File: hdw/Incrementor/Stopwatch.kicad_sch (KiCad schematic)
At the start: 0 parts

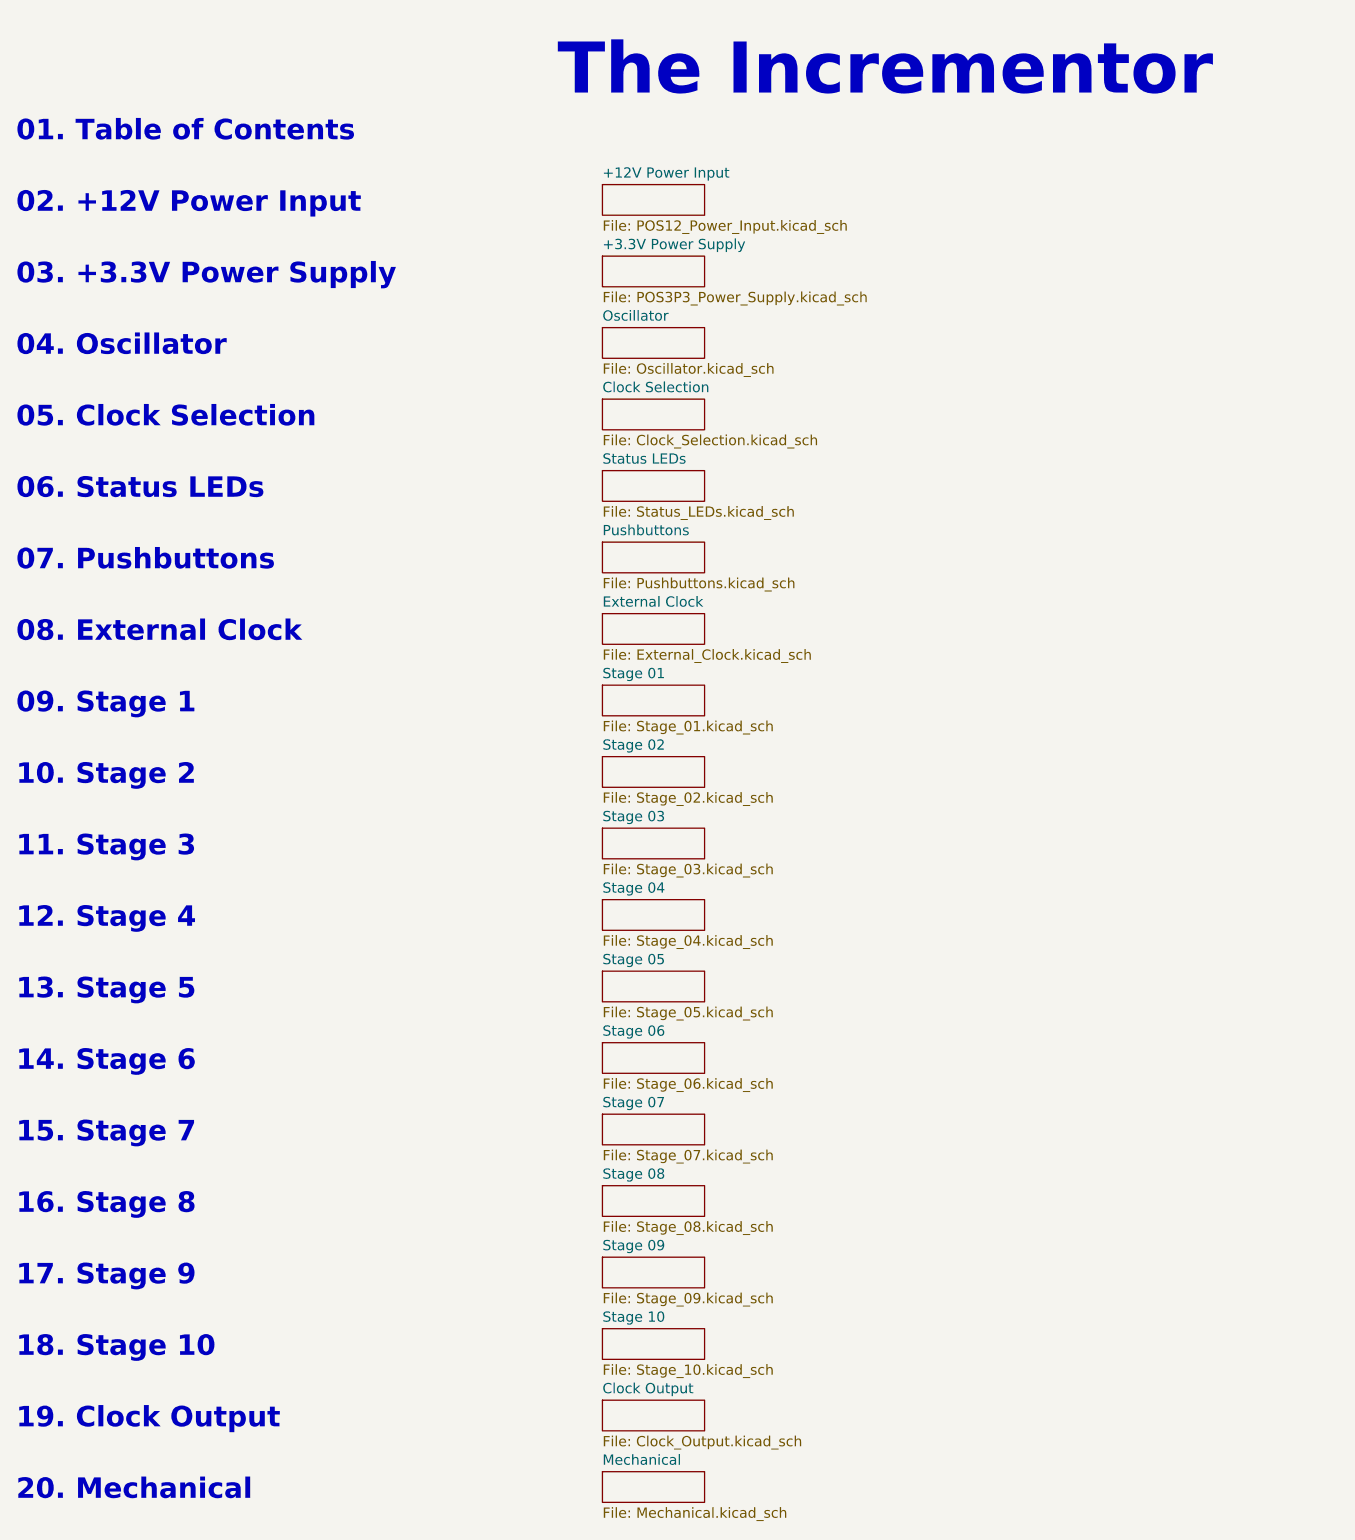
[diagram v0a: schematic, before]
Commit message: renamed project, removed stuff I dont need
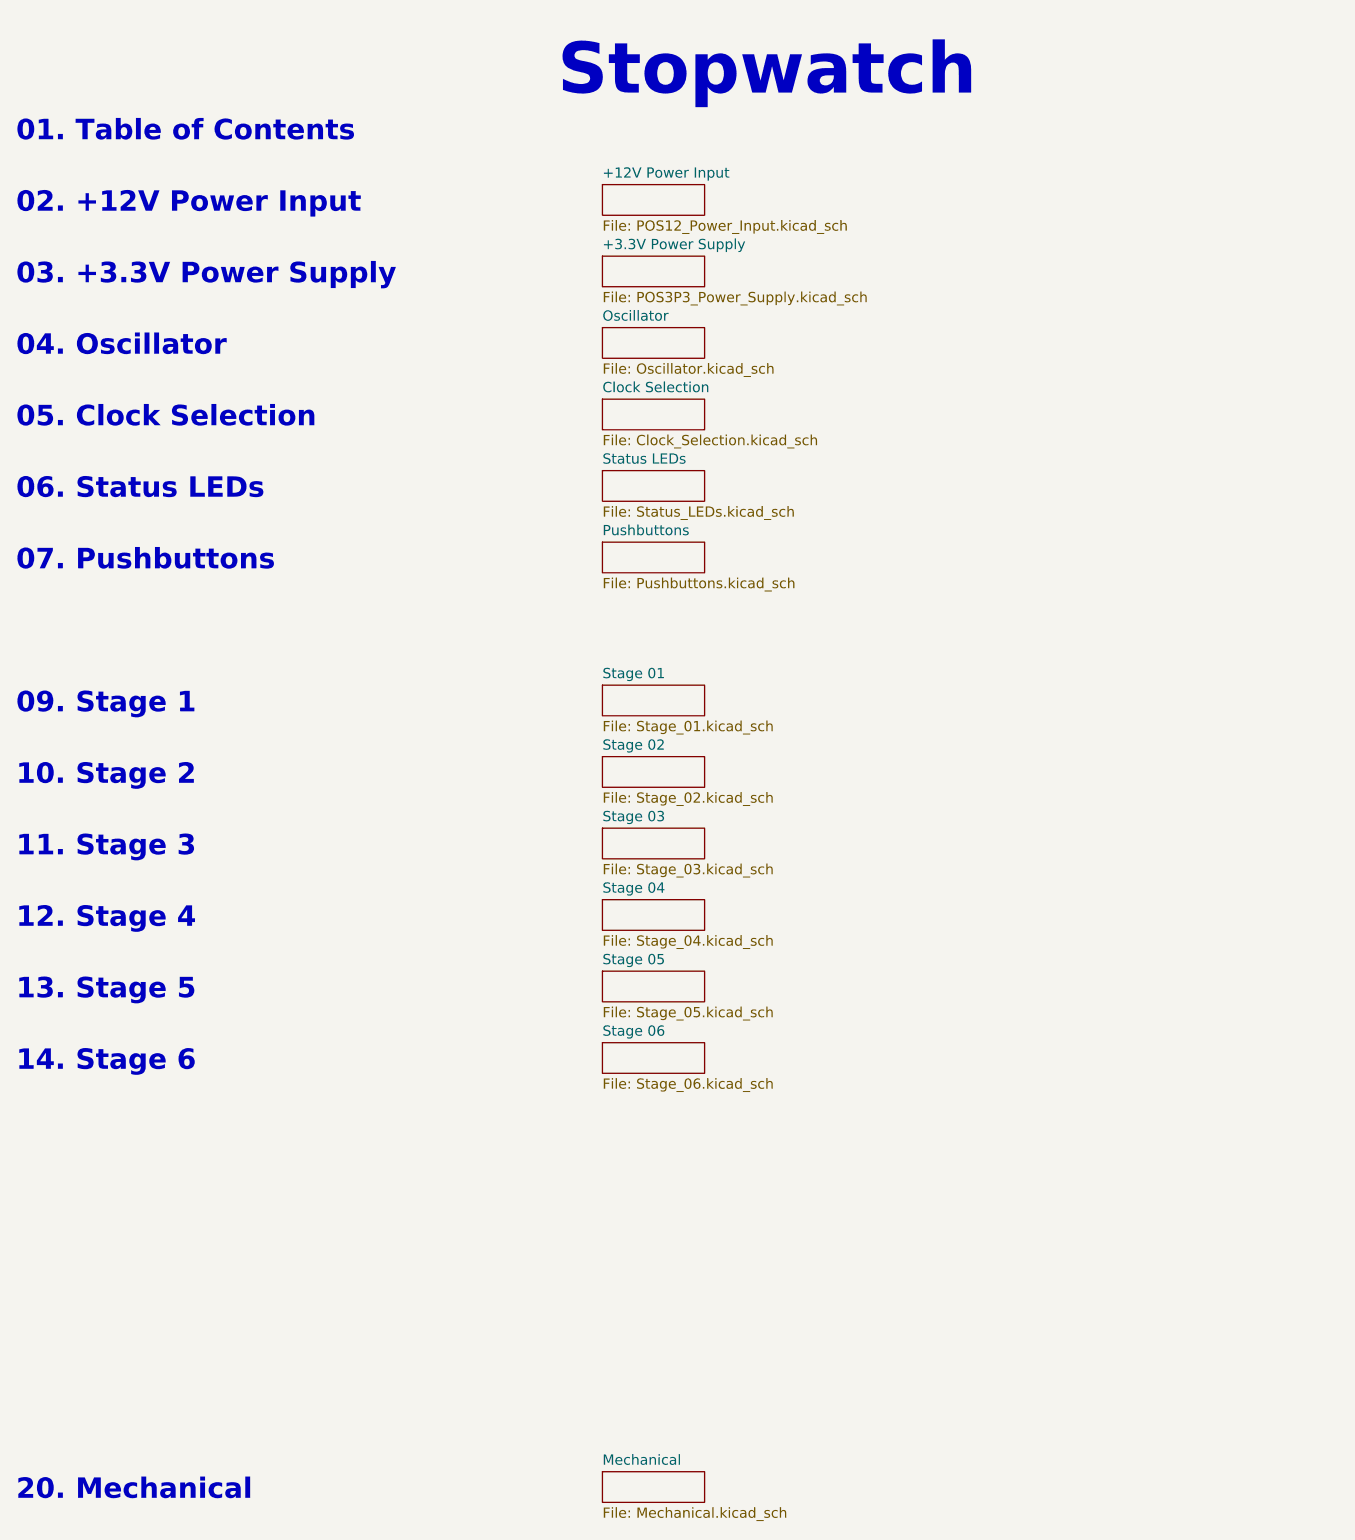
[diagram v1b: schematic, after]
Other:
- removed sheet Clock Output
- removed sheet External Clock
- removed sheet Stage 07
- removed sheet Stage 08
- removed sheet Stage 09
- removed sheet Stage 10
- note added: "Stopwatch"
- note removed: "08. External Clock"
- note removed: "15. Stage 7"
- note removed: "16. Stage 8"
- note removed: "17. Stage 9"
- note removed: "18. Stage 10"
- note removed: "19. Clock Output"
- note removed: "The Incrementor"
- title: Incrementor -> Stopwatch
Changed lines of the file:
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@@
   (paper "A")
   (title_block
-    (title "Incrementor")
-    (date "2019-09-03")
+    (title "Stopwatch")
+    (date "2024-01-02")
     (rev "A")
     (company "Drew Maatman")
@@
     (effects (font (size 2.54 2.54) (thickness 0.508) bold) (justify left bottom))
   )
-  (text "18. Stage 10" (at 29.972 179.832 0)
-    (effects (font (size 2.54 2.54) (thickness 0.508) bold) (justify left bottom))
-  )
-  (text "17. Stage 9" (at 29.972 170.942 0)
-    (effects (font (size 2.54 2.54) (thickness 0.508) bold) (justify left bottom))
-  )
   (text "11. Stage 3" (at 29.972 117.602 0)
     (effects (font (size 2.54 2.54) (thickness 0.508) bold) (justify left bottom))
   )
-  (text "19. Clock Output" (at 29.972 188.722 0)
-    (effects (font (size 2.54 2.54) (thickness 0.508) bold) (justify left bottom))
-  )
   (text "06. Status LEDs" (at 29.972 73.152 0)
     (effects (font (size 2.54 2.54) (thickness 0.508) bold) (justify left bottom))
   )
-  (text "08. External Clock" (at 29.972 90.932 0)
-    (effects (font (size 2.54 2.54) (thickness 0.508) bold) (justify left bottom))
-  )
   (text "20. Mechanical" (at 29.972 197.612 0)
     (effects (font (size 2.54 2.54) (thickness 0.508) bold) (justify left bottom))
@@
     (effects (font (size 2.54 2.54) (thickness 0.508) bold) (justify left bottom))
   )
-  (text "16. Stage 8" (at 29.972 162.052 0)
-    (effects (font (size 2.54 2.54) (thickness 0.508) bold) (justify left bottom))
-  )
-  (text "15. Stage 7" (at 29.972 153.162 0)
-    (effects (font (size 2.54 2.54) (thickness 0.508) bold) (justify left bottom))
-  )
-  (text "The Incrementor" (at 97.282 23.368 0)
+  (text "Stopwatch" (at 97.282 23.368 0)
     (effects (font (size 6.35 6.35) (thickness 1.27) bold) (justify left bottom))
   )
@@
     )
     (instances
-      (project "Incrementor"
+      (project "Stopwatch"
         (path "/c0d2575b-aec2-49ed-8c32-97fe6e68824c" (page "9"))
       )
@@
     )
     (instances
-      (project "Incrementor"
+      (project "Stopwatch"
         (path "/c0d2575b-aec2-49ed-8c32-97fe6e68824c" (page "10"))
       )
@@
     )
     (instances
-      (project "Incrementor"
+      (project "Stopwatch"
         (path "/c0d2575b-aec2-49ed-8c32-97fe6e68824c" (page "11"))
       )
@@
     )
     (instances
-      (project "Incrementor"
+      (project "Stopwatch"
         (path "/c0d2575b-aec2-49ed-8c32-97fe6e68824c" (page "12"))
       )
@@
     )
     (instances
-      (project "Incrementor"
+      (project "Stopwatch"
         (path "/c0d2575b-aec2-49ed-8c32-97fe6e68824c" (page "13"))
       )
@@
     )
     (instances
-      (project "Incrementor"
+      (project "Stopwatch"
         (path "/c0d2575b-aec2-49ed-8c32-97fe6e68824c" (page "14"))
       )
     )
   )
-  (sheet (at 102.87 149.352) (size 12.7 3.81) (fields_autoplaced)
-    (stroke (width 0) (type solid))
-    (fill (color 0 0 0 0.0000))
-    (property "Sheetname" "Stage 07" (at 102.87 148.6404 0)
-      (effects (font (size 1.27 1.27)) (justify left bottom))
-    )
-    (property "Sheetfile" "Stage_07.kicad_sch" (at 102.87 153.7466 0)
-      (effects (font (size 1.27 1.27)) (justify left top))
-    )
-    (instances
-      (project "Incrementor"
-        (path "/c0d2575b-aec2-49ed-8c32-97fe6e68824c" (page "15"))
-      )
-    )
-  )
-  (sheet (at 102.87 158.242) (size 12.7 3.81) (fields_autoplaced)
-    (stroke (width 0) (type solid))
-    (fill (color 0 0 0 0.0000))
-    (property "Sheetname" "Stage 08" (at 102.87 157.5304 0)
-      (effects (font (size 1.27 1.27)) (justify left bottom))
-    )
-    (property "Sheetfile" "Stage_08.kicad_sch" (at 102.87 162.6366 0)
-      (effects (font (size 1.27 1.27)) (justify left top))
-    )
-    (instances
-      (project "Incrementor"
-        (path "/c0d2575b-aec2-49ed-8c32-97fe6e68824c" (page "16"))
-      )
-    )
-  )
-  (sheet (at 102.87 167.132) (size 12.7 3.81) (fields_autoplaced)
-    (stroke (width 0) (type solid))
-    (fill (color 0 0 0 0.0000))
-    (property "Sheetname" "Stage 09" (at 102.87 166.4204 0)
-      (effects (font (size 1.27 1.27)) (justify left bottom))
-    )
-    (property "Sheetfile" "Stage_09.kicad_sch" (at 102.87 171.5266 0)
-      (effects (font (size 1.27 1.27)) (justify left top))
-    )
-    (instances
-      (project "Incrementor"
-        (path "/c0d2575b-aec2-49ed-8c32-97fe6e68824c" (page "17"))
-      )
-    )
-  )
-  (sheet (at 102.87 176.022) (size 12.7 3.81) (fields_autoplaced)
-    (stroke (width 0) (type solid))
-    (fill (color 0 0 0 0.0000))
-    (property "Sheetname" "Stage 10" (at 102.87 175.3104 0)
-      (effects (font (size 1.27 1.27)) (justify left bottom))
-    )
-    (property "Sheetfile" "Stage_10.kicad_sch" (at 102.87 180.4166 0)
-      (effects (font (size 1.27 1.27)) (justify left top))
-    )
-    (instances
-      (project "Incrementor"
-        (path "/c0d2575b-aec2-49ed-8c32-97fe6e68824c" (page "18"))
-      )
-    )
-  )
   (sheet (at 102.87 60.452) (size 12.7 3.81) (fields_autoplaced)
     (stroke (width 0) (type solid))
@@
     )
     (instances
-      (project "Incrementor"
+      (project "Stopwatch"
         (path "/c0d2575b-aec2-49ed-8c32-97fe6e68824c" (page "5"))
       )
@@
     )
     (instances
-      (project "Incrementor"
+      (project "Stopwatch"
         (path "/c0d2575b-aec2-49ed-8c32-97fe6e68824c" (page "6"))
       )
@@
     )
     (instances
-      (project "Incrementor"
+      (project "Stopwatch"
         (path "/c0d2575b-aec2-49ed-8c32-97fe6e68824c" (page "7"))
       )
     )
   )
-  (sheet (at 102.87 87.122) (size 12.7 3.81) (fields_autoplaced)
-    (stroke (width 0) (type solid))
-    (fill (color 0 0 0 0.0000))
-    (property "Sheetname" "External Clock" (at 102.87 86.4104 0)
-      (effects (font (size 1.27 1.27)) (justify left bottom))
-    )
-    (property "Sheetfile" "External_Clock.kicad_sch" (at 102.87 91.5166 0)
-      (effects (font (size 1.27 1.27)) (justify left top))
-    )
-    (instances
-      (project "Incrementor"
-        (path "/c0d2575b-aec2-49ed-8c32-97fe6e68824c" (page "8"))
-      )
-    )
-  )
-  (sheet (at 102.87 184.912) (size 12.7 3.81) (fields_autoplaced)
-    (stroke (width 0) (type solid))
-    (fill (color 0 0 0 0.0000))
-    (property "Sheetname" "Clock Output" (at 102.87 184.2004 0)
-      (effects (font (size 1.27 1.27)) (justify left bottom))
-    )
-    (property "Sheetfile" "Clock_Output.kicad_sch" (at 102.87 189.3066 0)
-      (effects (font (size 1.27 1.27)) (justify left top))
-    )
-    (instances
-      (project "Incrementor"
-        (path "/c0d2575b-aec2-49ed-8c32-97fe6e68824c" (page "19"))
-      )
-    )
-  )
   (sheet (at 102.87 42.672) (size 12.7 3.81) (fields_autoplaced)
     (stroke (width 0) (type solid))
@@
     )
     (instances
-      (project "Incrementor"
+      (project "Stopwatch"
         (path "/c0d2575b-aec2-49ed-8c32-97fe6e68824c" (page "3"))
       )
@@
     )
     (instances
-      (project "Incrementor"
+      (project "Stopwatch"
         (path "/c0d2575b-aec2-49ed-8c32-97fe6e68824c" (page "2"))
       )
@@
     )
     (instances
-      (project "Incrementor"
+      (project "Stopwatch"
         (path "/c0d2575b-aec2-49ed-8c32-97fe6e68824c" (page "20"))
       )
@@
     )
     (instances
-      (project "Incrementor"
+      (project "Stopwatch"
         (path "/c0d2575b-aec2-49ed-8c32-97fe6e68824c" (page "4"))
       )
